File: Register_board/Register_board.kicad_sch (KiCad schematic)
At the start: 118 parts, among them J1 Conn_02x30_Odd_Even, U1 74LS374, U10 74LS244, U11 74LS194, U12 74LS181, U13 74LS181, U14 74LS194, U15 74LS244, U18 74LS77, U2 74LS374, U3 74LS374, U4 74LS374, U5 74LS374, U6 74LS374, U7 74LS374, U8 74LS374, U9 74LS244

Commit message: Register board schematic
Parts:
- removed R48: 10K, Resistor_SMD:R_0603_1608Metric_Pad0.98x0.95mm_HandSolder, symbol Device:R
- removed U11, U14: 74LS194, Package_DIP:DIP-16_W7.62mm_Socket, symbol 74xx:74LS194
- removed U18: 74LS77, Package_DIP:DIP-12_W7.62mm_Socket, symbol 74xx:74LS77
- added C16: 100nF, Capacitor_SMD:C_0603_1608Metric_Pad1.08x0.95mm_HandSolder, symbol Device:C
- added D14, D15, D16, D17, D30, D31: LED, LED_SMD:LED_0603_1608Metric_Pad1.05x0.95mm_HandSolder, symbol Device:LED
- added NT1: NetTie_2, symbol Device:NetTie_2
- added R14, R15, R16, R21, R26, R27, R28, R29, R30, R31, R32, R33, R34, R35, R52, R53, R54, R55, R56, R57, R58, R59, R60, R61, R62, R63, R64, R65, R66, R67, R85, R86, R91, R92, R96: 10K, Resistor_SMD:R_0603_1608Metric_Pad0.98x0.95mm_HandSolder, symbol Device:R
- added R17, R18, R19, R20, R46: 330R, Resistor_SMD:R_0603_1608Metric_Pad0.98x0.95mm_HandSolder, symbol Device:R
- added U12, U13: 74LS374, Package_DIP:DIP-20_W7.62mm_Socket, symbol 74xx:74LS374
- added U16: 74LS75, Package_DIP:DIP-16_W7.62mm_Socket, symbol 74xx:74LS75
- R47: value 10K -> 330R
- renumbered D9 to D10, D10 to D11, D14 to D18, D15 to D19, D16 to D20, D17 to D21, D18 to D22, D19 to D23, D20 to D24, D21 to D25, D25 to D26, D23 to D27, D24 to D28, D22 to D29, D5 to D3, D26 to D32, D27 to D33, D28 to D34, D29 to D35, D3 to D4, D4 to D5, D11 to D9, R9 to R10, R10 to R11, R14 to R22, R15 to R23, R5 to R3, R30 to R36, R31 to R37, R32 to R38, R33 to R39, R3 to R4, R34 to R40, R35 to R41, R39 to R42, R37 to R43, R38 to R44, R36 to R45, R40 to R48, R41 to R49, R4 to R5, R42 to R50, R43 to R51, R16 to R68, R17 to R69, R18 to R70, R19 to R71, R20 to R72, R21 to R73, R22 to R74, R23 to R75, R49 to R76, R50 to R77, R51 to R78, R52 to R79, R53 to R80, R54 to R81, R55 to R82, R56 to R83, R57 to R84, R26 to R87, R27 to R88, R28 to R89, R11 to R9, R29 to R90, R44 to R93, R45 to R94, R46 to R95, U15 to U11, U13 to U14, U12 to U15
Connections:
- net ACC_S1 is gone; now on net ALU_S1: D21.2 (A)
- net ~{FLAGS_A_UPDATE} is gone; now on net FLAGS_A_UPDATE: D27.1 (K), R94.1
- net ~{FLAGS_B_UPDATE} is gone; now on net FLAGS_B_UPDATE: D28.1 (K), R95.1
- net +5V: now also R47.2, C16.1, R17.2, R18.2, R91.2, R92.2, R96.2, U12.20 (VCC), U13.20 (VCC), U16.5 (VCC)
- net A0: now also R14.2
- net A1: now also R15.2
- net A10: now also R30.2
- net A11: now also R31.2
- net A12: now also R32.2
- net A13: now also R33.2
- net A14: now also R34.2
- net A15: now also R35.2
- net A2: now also R16.2
- net A3: now also R21.2
- net A4: now also R24.2
- net A5: now also R25.2
- net A6: now also R26.2
- net A7: now also R27.2
- net A8: now also R28.2
- net A9: now also R29.2
- net ALU_M: now also J1.34 (Pin_34)
- net ALU_S0: now also D20.2 (A), J1.26 (Pin_26)
- net ALU_S1: now also J1.28 (Pin_28)
- net ALU_S2: now also J1.30 (Pin_30)
- net ALU_S3: now also J1.32 (Pin_32), D30.2 (A)
- net CARRY_FLAG_A: now also J1.42 (Pin_42), U16.1 (~{Q0})
- net CARRY_FLAG_B: now also J1.46 (Pin_46), U16.11 (~{Q2})
- net CLK: no longer R25.1
- net D0: now also R53.2, U13.2 (O0); no longer U1.3 (D0), U10.18 (O0a), U2.3 (D0), U3.3 (D0), U4.3 (D0), U5.3 (D0), U6.3 (D0), U7.3 (D0), U8.3 (D0), U9.18 (O0a)
- net D1: now also R55.2, U13.5 (O1); no longer U1.4 (D1), U10.16 (O1a), U2.4 (D1), U3.4 (D1), U4.4 (D1), U5.4 (D1), U6.4 (D1), U7.4 (D1), U8.4 (D1), U9.16 (O1a)
- net D2: now also R57.2, U13.6 (O2); no longer U1.7 (D2), U10.14 (O2a), U2.7 (D2), U3.7 (D2), U4.7 (D2), U5.7 (D2), U6.7 (D2), U7.7 (D2), U8.7 (D2), U9.14 (O2a)
- net D3: now also R59.2, U13.9 (O3); no longer U1.8 (D3), U10.12 (O3a), U2.8 (D3), U3.8 (D3), U4.8 (D3), U5.8 (D3), U6.8 (D3), U7.8 (D3), U8.8 (D3), U9.12 (O3a)
- net D4: now also R61.2, U13.12 (O4); no longer U1.13 (D4), U10.9 (O0b), U2.13 (D4), U3.13 (D4), U4.13 (D4), U5.13 (D4), U6.13 (D4), U7.13 (D4), U8.13 (D4), U9.9 (O0b)
- net D5: now also R63.2, U13.15 (O5); no longer U1.14 (D5), U10.7 (O1b), U2.14 (D5), U3.14 (D5), U4.14 (D5), U5.14 (D5), U6.14 (D5), U7.14 (D5), U8.14 (D5), U9.7 (O1b)
- net D6: now also R65.2, U13.16 (O6); no longer U1.17 (D6), U10.5 (O2b), U2.17 (D6), U3.17 (D6), U4.17 (D6), U5.17 (D6), U6.17 (D6), U7.17 (D6), U8.17 (D6), U9.5 (O2b)
- net D7: now also R67.2, U13.19 (O7); no longer U1.18 (D7), U10.3 (O3b), U2.18 (D7), U3.18 (D7), U4.18 (D7), U5.18 (D7), U6.18 (D7), U7.18 (D7), U8.18 (D7), U9.3 (O3b)
- net EQUAL_FLAG_A: now also J1.44 (Pin_44), U16.15 (Q1)
- net EQUAL_FLAG_B: now also J1.48 (Pin_48), U16.9 (Q3)
- net GND: now also R24.1, R25.1, C16.2, R14.1, R15.1, R16.1, R19.2, R20.2, R21.1, R26.1, R27.1, R28.1, R29.1, R30.1, R31.1, R32.1, R33.1, R34.1, R35.1, R46.2, R52.1, R53.1, R54.1, R55.1, R56.1, R57.1, R58.1, R59.1, R60.1, R61.1, R62.1, R63.1, R64.1, R65.1, R66.1, R67.1, R85.2, R86.2, U12.10 (GND), U13.10 (GND), U16.12 (GND); no longer R24.2, R25.2, R47.2
- net ~{ALU_CIN}: now also J1.36 (Pin_36)
- net ALU1: now reaches U11.4 (I1a), U14.10 (F1)
- net ALU1: now also U1.4 (D1), U2.4 (D1), U3.4 (D1), U4.4 (D1), U5.4 (D1), U6.4 (D1), U7.4 (D1), U8.4 (D1), U12.4 (D1), U13.4 (D1)
- net ALU2: now reaches U11.6 (I2a), U14.11 (F2)
- net ALU2: now also U1.7 (D2), U2.7 (D2), U3.7 (D2), U4.7 (D2), U5.7 (D2), U6.7 (D2), U7.7 (D2), U8.7 (D2), U12.7 (D2), U13.7 (D2)
- net ALU3: now reaches U11.8 (I3a), U14.13 (F3)
- net ALU3: now also U1.8 (D3), U2.8 (D3), U3.8 (D3), U4.8 (D3), U5.8 (D3), U6.8 (D3), U7.8 (D3), U8.8 (D3), U12.8 (D3), U13.8 (D3)
- net at U14.14 (A=B): now also NT1.1; no longer U15.14 (A=B)
- net L3: now reaches U14.19 (A3)
- net L3: now also U10.12 (O3a), U9.12 (O3a), R58.2, U12.9 (O3)
- net L0: now reaches U14.2 (A0)
- net L0: now also U10.18 (O0a), U9.18 (O0a), R52.2, U12.2 (O0)
- net L2: now reaches U14.21 (A2)
- net L2: now also U10.14 (O2a), U9.14 (O2a), R56.2, U12.6 (O2)
- net L1: now reaches U14.23 (A1)
- net L1: now also U10.16 (O1a), U9.16 (O1a), R54.2, U12.5 (O1)
- net ALU0: now reaches U11.2 (I0a), U14.9 (F0)
- net ALU0: now also U1.3 (D0), U2.3 (D0), U3.3 (D0), U4.3 (D0), U5.3 (D0), U6.3 (D0), U7.3 (D0), U8.3 (D0), U12.3 (D0), U13.3 (D0)
- net ALU5: now reaches U11.13 (I1b), U15.10 (F1)
- net ALU5: now also U1.14 (D5), U2.14 (D5), U3.14 (D5), U4.14 (D5), U5.14 (D5), U6.14 (D5), U7.14 (D5), U8.14 (D5), U12.14 (D5), U13.14 (D5)
- net ALU6: now reaches U11.15 (I2b), U15.11 (F2)
- net ALU6: now also U1.17 (D6), U2.17 (D6), U3.17 (D6), U4.17 (D6), U5.17 (D6), U6.17 (D6), U7.17 (D6), U8.17 (D6), U12.17 (D6), U13.17 (D6)
- net ALU7: now reaches U11.17 (I3b), U15.13 (F3)
- net ALU7: now also U1.18 (D7), U2.18 (D7), U3.18 (D7), U4.18 (D7), U5.18 (D7), U6.18 (D7), U7.18 (D7), U8.18 (D7), U12.18 (D7), U13.18 (D7)
- net at U15.16 (Cn+4): now also U16.2 (D0), U16.6 (D2)
- net L7: now reaches U15.19 (A3)
- net L7: now also U10.3 (O3b), U9.3 (O3b), R66.2, U12.19 (O7)
- net L4: now reaches U15.2 (A0)
- net L4: now also U10.9 (O0b), U9.9 (O0b), R60.2, U12.12 (O4)
- net L6: now reaches U15.21 (A2)
- net L6: now also U10.5 (O2b), U9.5 (O2b), R64.2, U12.16 (O6)
- net L5: now reaches U15.23 (A1)
- net L5: now also U10.7 (O1b), U9.7 (O1b), R62.2, U12.15 (O5)
- net ALU4: now reaches U11.11 (I0b), U15.9 (F0)
- net ALU4: now also U1.13 (D4), U2.13 (D4), U3.13 (D4), U4.13 (D4), U5.13 (D4), U6.13 (D4), U7.13 (D4), U8.13 (D4), U12.13 (D4), U13.13 (D4)
- net ~{ALU_OUT}: now reaches U11.1 (OEa)
- net ~{ALU_OUT}: now also J1.54 (Pin_54), U11.19 (OEb), D31.1 (K), R96.1
- net FLAGS_A_UPDATE: now reaches J1.38 (Pin_38)
- net FLAGS_A_UPDATE: now also U16.13 (E01)
- net FLAGS_B_UPDATE: now reaches J1.40 (Pin_40)
- net FLAGS_B_UPDATE: now also U16.4 (E23)
- net A_LOAD: now reaches J1.50 (Pin_50)
- net A_LOAD: now also D16.2 (A), R85.1, U12.11 (Cp)
- net T_LOAD: now reaches J1.52 (Pin_52)
- net T_LOAD: now also D17.2 (A), R86.1, U13.11 (Cp)
- net ~{A_OUT}: now reaches J1.53 (Pin_53)
- net ~{A_OUT}: now also D14.1 (K), R91.1, U12.1 (OE)
- net ~{T_OUT}: now reaches J1.55 (Pin_55)
- net ~{T_OUT}: now also D15.1 (K), R92.1, U13.1 (OE)
- net ACC_S0: no longer names the net of R47.1
- net ACC_S0: now also D31.2 (A); no longer D20.2 (A)
- net RESET renamed ~{RESET}
- net ~{RESET}: no longer R24.1
- new net: D15.2 (A), R18.1
- new net: D17.1 (K), R20.1
- new net: NT1.2, U15.14 (A=B), U16.3 (D1), U16.7 (D3)
- new net: D30.1 (K), R46.1
- new net: D14.2 (A), R17.1
- new net: D16.1 (K), R19.1
- no-connect marks 24 -> 11
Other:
- note added: "Latch bad, could cause control roms to oscilate Saves a chip over proper flip flops though"
- moved on the sheet: C1, C10, C11, C12, C13, C14, C15, C2, C3, C4, C5, C6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

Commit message: Register board
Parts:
- removed C1, C10, C11, C12, C13, C14, C15, C16, C2, C3, C4, C5, C6, C7, C8, C9: 100nF, Capacitor_SMD:C_0603_1608Metric_Pad1.08x0.95mm_HandSolder, symbol Device:C
- removed D10, D11, D12, D13, D14, D15, D16, D17, D18, D19, D2, D20, D21, D22, D23, D24, D25, D26, D27, D28, D29, D3, D30, D31, D32, D33, D34, D35, D4, D5, D6, D7, D8, D9: LED, LED_SMD:LED_0603_1608Metric_Pad1.05x0.95mm_HandSolder, symbol Device:LED
- removed R10, R11, R12, R13, R17, R18, R19, R2, R20, R22, R23, R3, R36, R37, R38, R39, R4, R40, R41, R42, R43, R44, R45, R46, R47, R48, R49, R5, R50, R51, R6, R7, R8, R9: 330R, Resistor_SMD:R_0603_1608Metric_Pad0.98x0.95mm_HandSolder, symbol Device:R
- removed R14, R15, R16, R21, R24, R25, R26, R27, R28, R29, R30, R31, R32, R33, R34, R35, R52, R53, R54, R55, R56, R57, R58, R59, R60, R61, R62, R63, R64, R65, R66, R67, R68, R69, R70, R71, R72, R73, R74, R75, R76, R77, R78, R79, R80, R81, R82, R83, R84, R85, R86, R87, R88, R89, R90, R91, R92, R93, R94, R95, R96: 10K, Resistor_SMD:R_0603_1608Metric_Pad0.98x0.95mm_HandSolder, symbol Device:R
- added H1, H2, H3, H4: MountingHole, MountingHole:MountingHole_3.5mm, symbol Mechanical:MountingHole
- added RN1, RN2, RN3, RN4: R_Network08, Resistor_THT:R_Array_SIP9, symbol Device:R_Network08
- D1: footprint LED_SMD:LED_0603_1608Metric_Pad1.05x0.95mm_HandSolder -> LED_THT:LED_D3.0mm
- NT1: footprint (none) -> NetTie:NetTie-2_SMD_Pad0.5mm
- R1: footprint Resistor_SMD:R_0603_1608Metric_Pad0.98x0.95mm_HandSolder -> Resistor_THT:R_Axial_DIN0204_L3.6mm_D1.6mm_P2.54mm_Vertical
- U10: renamed from U14; footprint Package_DIP:DIP-24_W7.62mm_Socket -> Package_DIP:DIP-24_W15.24mm_Socket
- U11: renamed from U15; footprint Package_DIP:DIP-24_W7.62mm_Socket -> Package_DIP:DIP-24_W15.24mm_Socket
- renumbered U2 to U12, U4 to U13, U6 to U14, U8 to U15, U10 to U16, U3 to U2, U5 to U3, U7 to U4, U9 to U5, U12 to U6, U13 to U7, U11 to U8, U16 to U9
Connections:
- net +5V: now also J1.2 (Pin_2); no longer J1.60 (Pin_60)
- net A0: now also J1.53 (Pin_53), RN1.9 (R8); no longer J1.12 (Pin_12)
- net A1: now also J1.55 (Pin_55), RN1.7 (R6); no longer J1.11 (Pin_11)
- net A10: now also J1.58 (Pin_58), RN2.5 (R4); no longer J1.2 (Pin_2)
- net A11: now also J1.60 (Pin_60), RN2.3 (R2); no longer J1.1 (Pin_1)
- net A12: now also J1.47 (Pin_47), RN2.2 (R1); no longer J1.8 (Pin_8)
- net A13: now also J1.46 (Pin_46), RN2.4 (R3); no longer J1.7 (Pin_7)
- net A14: now also J1.45 (Pin_45), RN2.6 (R5); no longer J1.6 (Pin_6)
- net A15: now also J1.48 (Pin_48), RN2.8 (R7); no longer J1.5 (Pin_5)
- net A2: now also J1.57 (Pin_57), RN1.5 (R4); no longer J1.10 (Pin_10)
- net A3: now also J1.59 (Pin_59), RN1.3 (R2); no longer J1.9 (Pin_9)
- net A4: now also J1.49 (Pin_49), RN1.2 (R1); no longer J1.16 (Pin_16)
- net A5: now also J1.50 (Pin_50), RN1.4 (R3); no longer J1.15 (Pin_15)
- net A6: now also J1.51 (Pin_51), RN1.6 (R5); no longer J1.14 (Pin_14)
- net A7: now also J1.52 (Pin_52), RN1.8 (R7); no longer J1.13 (Pin_13)
- net A8: now also J1.54 (Pin_54), RN2.9 (R8); no longer J1.4 (Pin_4)
- net A9: now also J1.56 (Pin_56), RN2.7 (R6); no longer J1.3 (Pin_3)
- net ALU_M: now also J1.26 (Pin_26); no longer J1.34 (Pin_34)
- net ALU_S0: now also J1.21 (Pin_21); no longer J1.26 (Pin_26)
- net ALU_S1: now also J1.22 (Pin_22); no longer J1.28 (Pin_28)
- net ALU_S2: now also J1.19 (Pin_19); no longer J1.30 (Pin_30)
- net ALU_S3: now also J1.20 (Pin_20); no longer J1.32 (Pin_32)
- net A_LOAD: now also J1.17 (Pin_17); no longer J1.50 (Pin_50)
- net B_LOAD: now also J1.35 (Pin_35); no longer J1.39 (Pin_39)
- net CARRY_FLAG_A: now also J1.12 (Pin_12); no longer J1.42 (Pin_42)
- net CARRY_FLAG_B: now also J1.16 (Pin_16); no longer J1.46 (Pin_46)
- net CLK: now also J1.27 (Pin_27); no longer J1.58 (Pin_58)
- net C_LOAD: now also J1.31 (Pin_31); no longer J1.41 (Pin_41)
- net D0: now also J1.9 (Pin_9), RN4.9 (R8); no longer J1.20 (Pin_20)
- net D1: now also J1.10 (Pin_10), RN4.8 (R7); no longer J1.19 (Pin_19)
- net D2: now also J1.7 (Pin_7), RN4.7 (R6); no longer J1.18 (Pin_18)
- net D3: now also J1.8 (Pin_8), RN4.6 (R5); no longer J1.17 (Pin_17)
- net D4: now also J1.5 (Pin_5), RN4.5 (R4); no longer J1.24 (Pin_24)
- net D5: now also J1.6 (Pin_6), RN4.4 (R3); no longer J1.23 (Pin_23)
- net D6: now also J1.3 (Pin_3), RN4.3 (R2); no longer J1.22 (Pin_22)
- net D7: now also J1.4 (Pin_4), RN4.2 (R1); no longer J1.21 (Pin_21)
- net D_LOAD: now also J1.23 (Pin_23); no longer J1.45 (Pin_45)
- net EQUAL_FLAG_A: now also J1.11 (Pin_11); no longer J1.44 (Pin_44)
- net EQUAL_FLAG_B: now also J1.15 (Pin_15); no longer J1.48 (Pin_48)
- net E_LOAD: now also J1.30 (Pin_30); no longer J1.47 (Pin_47)
- net FLAGS_A_UPDATE: now also J1.14 (Pin_14); no longer J1.38 (Pin_38)
- net FLAGS_B_UPDATE: now also J1.13 (Pin_13); no longer J1.40 (Pin_40)
- net GND: now also J1.1 (Pin_1), RN1.1 (common), RN2.1 (common), RN3.1 (common), RN4.1 (common); no longer J1.59 (Pin_59)
- net L0: now also RN3.9 (R8)
- net L1: now also RN3.6 (R5)
- net L2: now also RN3.7 (R6)
- net L3: now also RN3.8 (R7)
- net L4: now also RN3.5 (R4)
- net L5: now also RN3.4 (R3)
- net L6: now also RN3.3 (R2)
- net L7: now also RN3.2 (R1)
- net PC_H_LOAD: now also J1.43 (Pin_43); no longer J1.27 (Pin_27)
- net PC_L_LOAD: now also J1.33 (Pin_33); no longer J1.29 (Pin_29)
- net SP_H_LOAD: now also J1.37 (Pin_37); no longer J1.33 (Pin_33)
- net SP_L_LOAD: now also J1.32 (Pin_32); no longer J1.35 (Pin_35)
- net T_LOAD: now also J1.18 (Pin_18); no longer J1.52 (Pin_52)
- net ~{ADR_H_OUT}: now also J1.38 (Pin_38); no longer J1.49 (Pin_49)
- net ~{ADR_L_OUT}: now also J1.25 (Pin_25); no longer J1.51 (Pin_51)
- net ~{ALU_CIN}: now also J1.24 (Pin_24); no longer J1.36 (Pin_36)
- net ~{ALU_OUT}: now also J1.41 (Pin_41); no longer J1.54 (Pin_54)
- net ~{A_OUT}: now also J1.39 (Pin_39); no longer J1.53 (Pin_53)
- net ~{BC_OUT}: now also J1.36 (Pin_36); no longer J1.37 (Pin_37)
- net ~{DE_OUT}: now also J1.34 (Pin_34); no longer J1.43 (Pin_43)
- net ~{PC_OUT}: now also J1.42 (Pin_42); no longer J1.25 (Pin_25)
- net ~{RESET}: now also J1.28 (Pin_28); no longer J1.57 (Pin_57)
- net ~{SP_OUT}: now also J1.44 (Pin_44); no longer J1.31 (Pin_31)
- net ~{T_OUT}: now also J1.40 (Pin_40); no longer J1.55 (Pin_55)
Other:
- moved on the sheet: D1

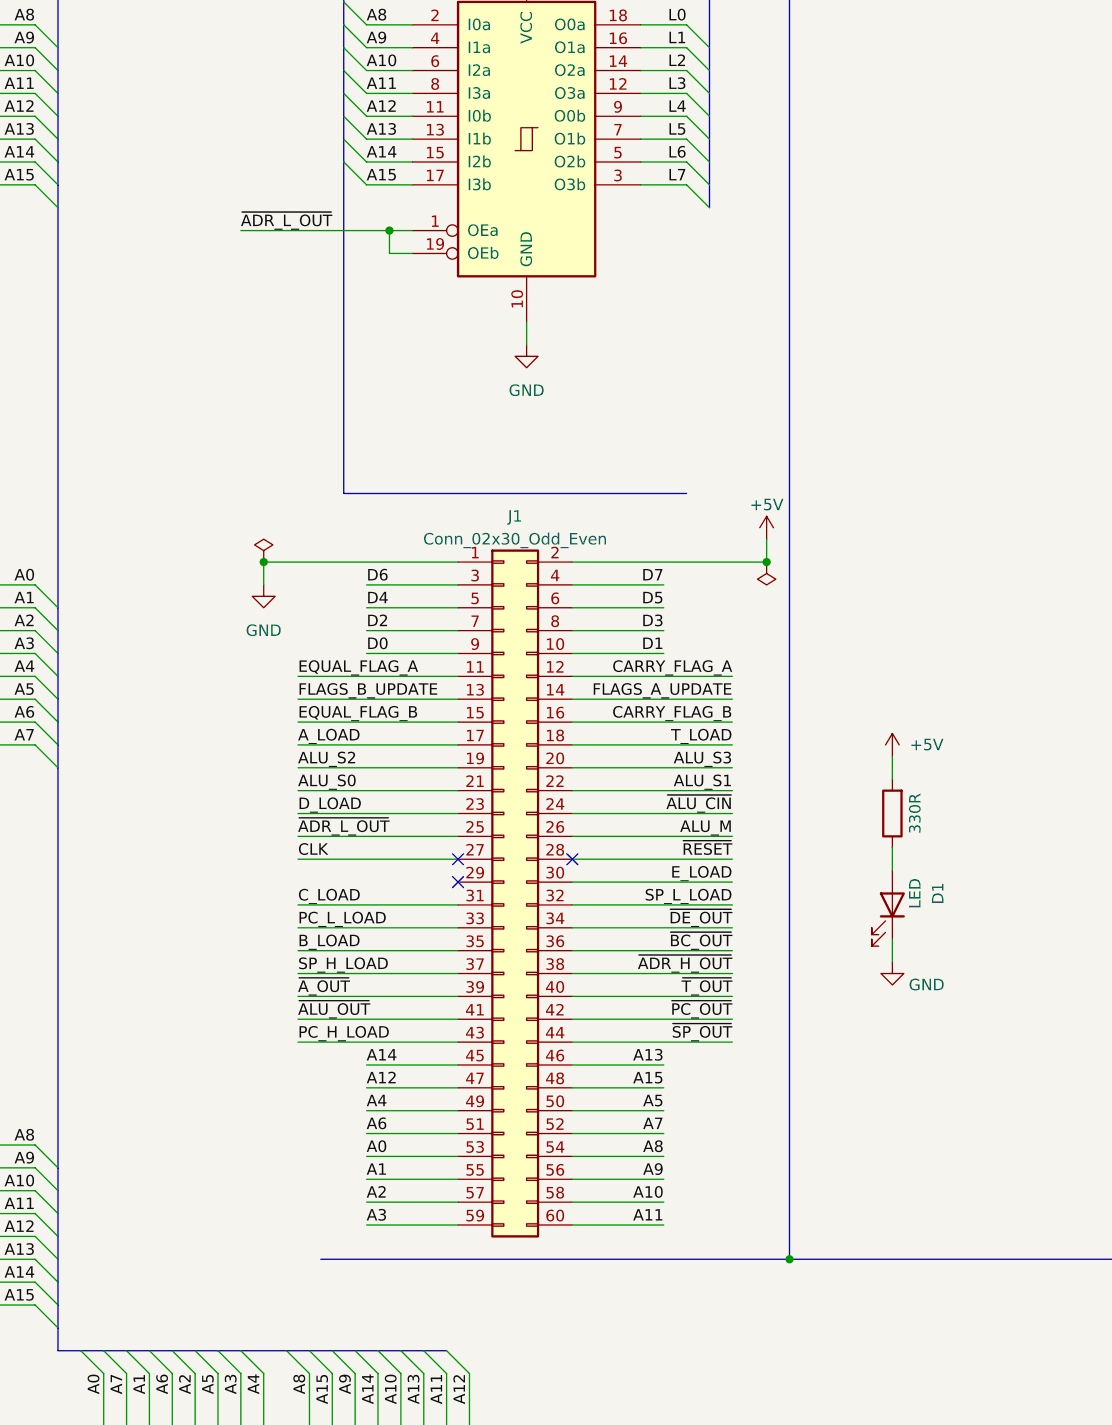
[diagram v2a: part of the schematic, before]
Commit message: Control panel schematic
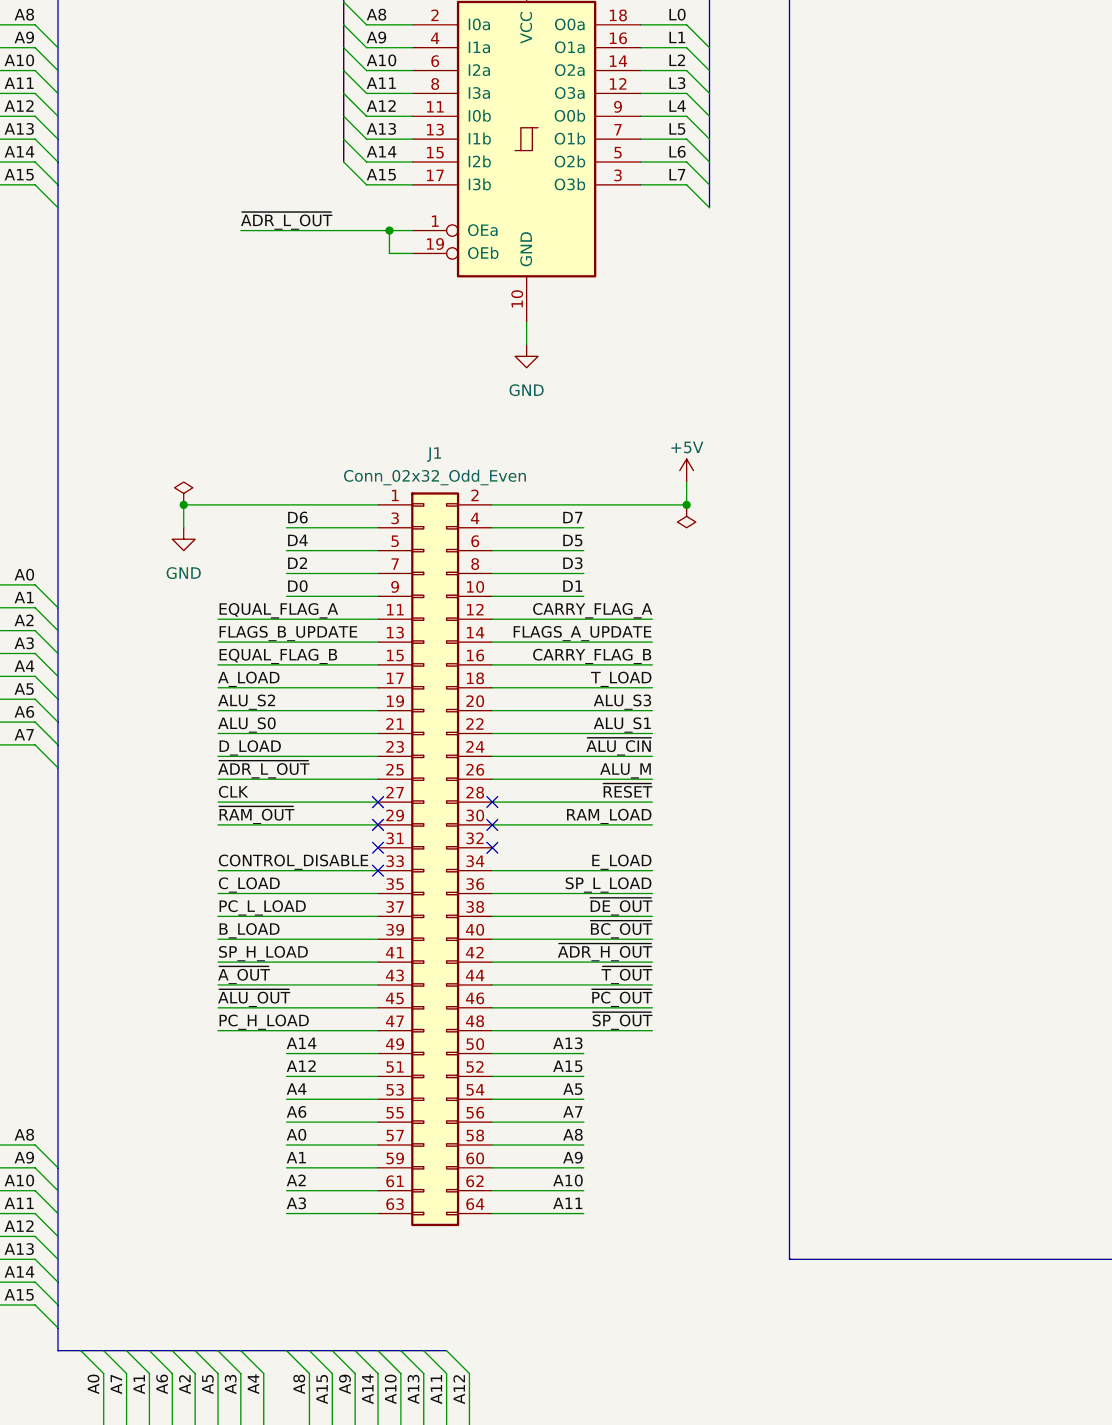
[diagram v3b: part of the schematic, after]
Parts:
- removed D1: LED, LED_THT:LED_D3.0mm, symbol Device:LED
- removed J1: Conn_02x30_Odd_Even, Connector_IDC:IDC-Header_2x30_P2.54mm_Vertical, symbol Connector_Generic:Conn_02x30_Odd_Even
- removed R1: 330R, Resistor_THT:R_Axial_DIN0204_L3.6mm_D1.6mm_P2.54mm_Vertical, symbol Device:R
- added J1: Conn_02x32_Odd_Even, Connector_IDC:IDC-Header_2x32_P2.54mm_Vertical, symbol Connector_Generic:Conn_02x32_Odd_Even
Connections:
- net +5V: now also J1.2 (Pin_2)
- net A0: now also J1.57 (Pin_57)
- net A1: now also J1.59 (Pin_59)
- net A10: now also J1.62 (Pin_62)
- net A11: now also J1.64 (Pin_64)
- net A12: now also J1.51 (Pin_51)
- net A13: now also J1.50 (Pin_50)
- net A14: now also J1.49 (Pin_49)
- net A15: now also J1.52 (Pin_52)
- net A2: now also J1.61 (Pin_61)
- net A3: now also J1.63 (Pin_63)
- net A4: now also J1.53 (Pin_53)
- net A5: now also J1.54 (Pin_54)
- net A6: now also J1.55 (Pin_55)
- net A7: now also J1.56 (Pin_56)
- net A8: now also J1.58 (Pin_58)
- net A9: now also J1.60 (Pin_60)
- net ALU_M: now also J1.26 (Pin_26)
- net ALU_S0: now also J1.21 (Pin_21)
- net ALU_S1: now also J1.22 (Pin_22)
- net ALU_S2: now also J1.19 (Pin_19)
- net ALU_S3: now also J1.20 (Pin_20)
- net A_LOAD: now also J1.17 (Pin_17)
- net B_LOAD: now also J1.39 (Pin_39)
- net CARRY_FLAG_A: now also J1.12 (Pin_12)
- net CARRY_FLAG_B: now also J1.16 (Pin_16)
- net CLK: now also J1.27 (Pin_27)
- net C_LOAD: now also J1.35 (Pin_35)
- net D0: now also J1.9 (Pin_9)
- net D1: now also J1.10 (Pin_10)
- net D2: now also J1.7 (Pin_7)
- net D3: now also J1.8 (Pin_8)
- net D4: now also J1.5 (Pin_5)
- net D5: now also J1.6 (Pin_6)
- net D6: now also J1.3 (Pin_3)
- net D7: now also J1.4 (Pin_4)
- net D_LOAD: now also J1.23 (Pin_23)
- net EQUAL_FLAG_A: now also J1.11 (Pin_11)
- net EQUAL_FLAG_B: now also J1.15 (Pin_15)
- net E_LOAD: now also J1.34 (Pin_34)
- net FLAGS_A_UPDATE: now also J1.14 (Pin_14)
- net FLAGS_B_UPDATE: now also J1.13 (Pin_13)
- net GND: now also J1.1 (Pin_1)
- net PC_H_LOAD: now also J1.47 (Pin_47)
- net PC_L_LOAD: now also J1.37 (Pin_37)
- net SP_H_LOAD: now also J1.41 (Pin_41)
- net SP_L_LOAD: now also J1.36 (Pin_36)
- net T_LOAD: now also J1.18 (Pin_18)
- net ~{ADR_H_OUT}: now also J1.42 (Pin_42)
- net ~{ADR_L_OUT}: now also J1.25 (Pin_25)
- net ~{ALU_CIN}: now also J1.24 (Pin_24)
- net ~{ALU_OUT}: now also J1.45 (Pin_45)
- net ~{A_OUT}: now also J1.43 (Pin_43)
- net ~{BC_OUT}: now also J1.40 (Pin_40)
- net ~{DE_OUT}: now also J1.38 (Pin_38)
- net ~{PC_OUT}: now also J1.46 (Pin_46)
- net ~{RESET}: now also J1.28 (Pin_28)
- net ~{SP_OUT}: now also J1.48 (Pin_48)
- net ~{T_OUT}: now also J1.44 (Pin_44)
- new net CONTROL_DISABLE: J1.33 (Pin_33)
- new net RAM_LOAD: J1.30 (Pin_30)
- new net ~{RAM_OUT}: J1.29 (Pin_29)
- no-connect marks 11 -> 15

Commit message: Register board and Control panel ordered
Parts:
- RN1, RN2, RN3, RN4: value R_Network08 -> 10K
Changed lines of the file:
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@@
       (effects (font (size 1.27 1.27)) (justify left))
     )
-    (property "Value" "R_Network08" (at 148.59 277.495 0)
+    (property "Value" "10K" (at 148.59 277.495 0)
       (effects (font (size 1.27 1.27)) (justify left))
     )
@@
       (effects (font (size 1.27 1.27)) (justify right))
     )
-    (property "Value" "R_Network08" (at 354.965 265.811 0)
+    (property "Value" "10K" (at 354.965 265.811 0)
       (effects (font (size 1.27 1.27)) (justify right))
     )
@@
       (effects (font (size 1.27 1.27)) (justify right))
     )
-    (property "Value" "R_Network08" (at 194.945 278.511 0)
+    (property "Value" "10K" (at 194.945 278.511 0)
       (effects (font (size 1.27 1.27)) (justify right))
     )
@@
       (effects (font (size 1.27 1.27)) (justify right))
     )
-    (property "Value" "R_Network08" (at 354.965 43.561 0)
+    (property "Value" "10K" (at 354.965 43.561 0)
       (effects (font (size 1.27 1.27)) (justify right))
     )
